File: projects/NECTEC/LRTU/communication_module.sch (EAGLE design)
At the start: 44 parts, among them Q1 BC847BS, U1 ESP-WROOM-32U (w/uFL), U2 IMAS980TH, U3 WG209_3E6, U4 RFM95W_SMT, X1 uFL, X2 uFL

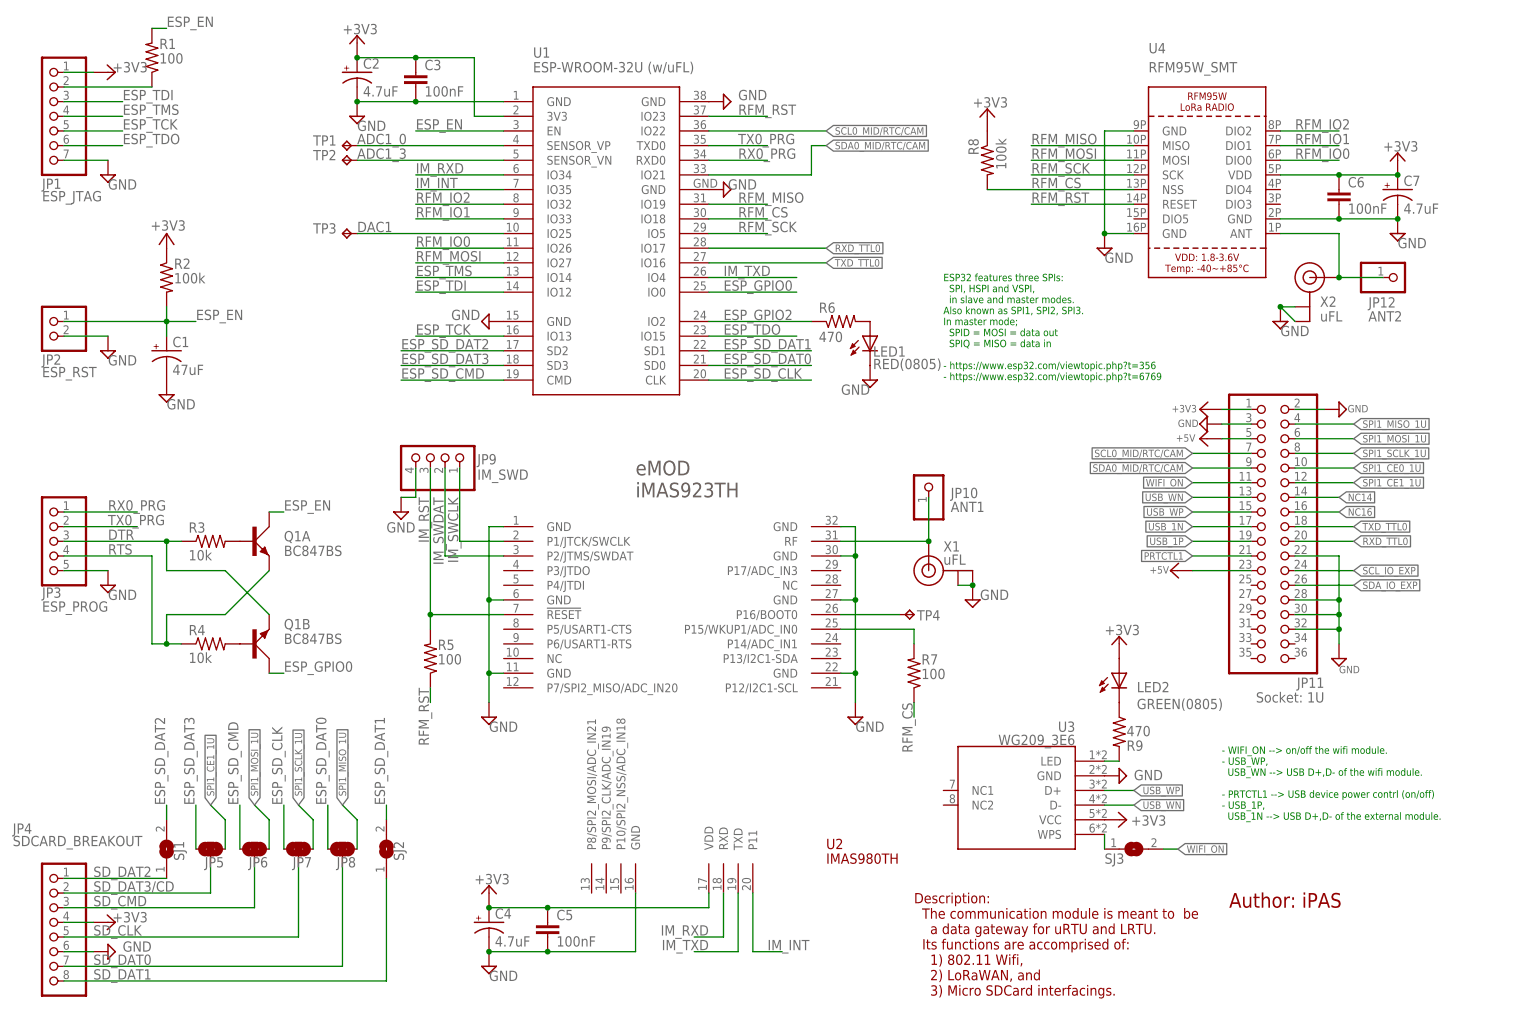
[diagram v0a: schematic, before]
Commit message: Fix ESP-eMOD connection, adding pull-up and swap uart pins.
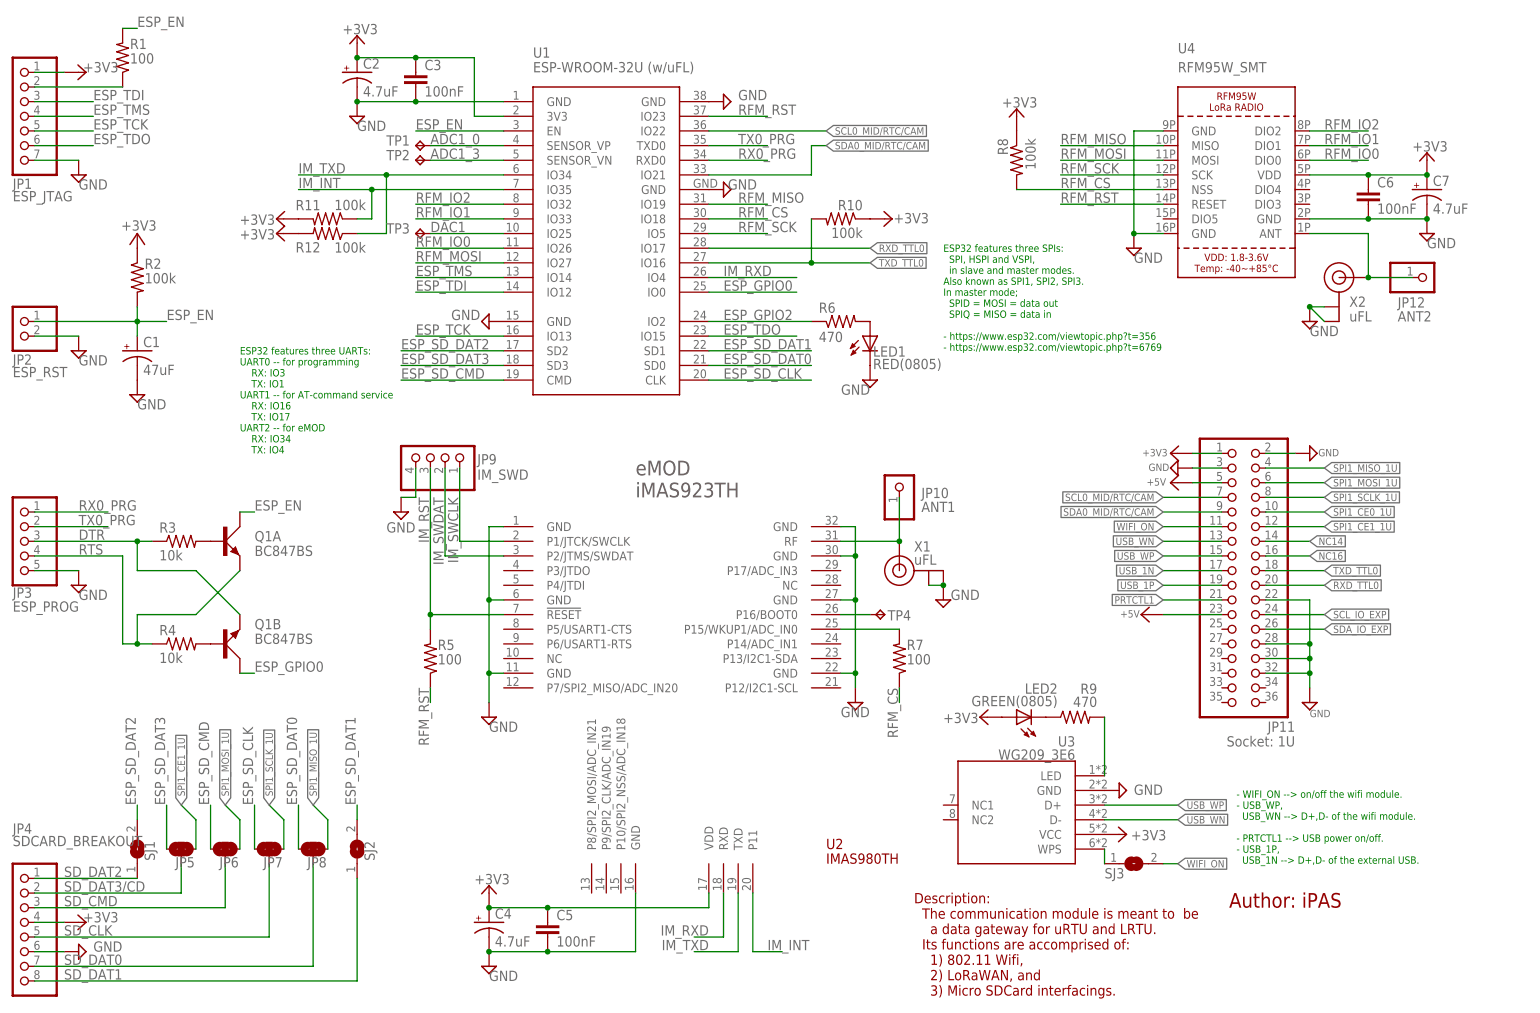
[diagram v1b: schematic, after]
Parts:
- added R10, R11, R12: 100k, ipas:RCL_R-USM0805
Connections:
- net +3V3: now also R10.1, R11.2, R12.2
- net IM_INT: now also R11.1
- net IM_RXD: now also U1.IO4; no longer U1.IO34
- net IM_TXD: now also R12.1, U1.IO34; no longer U1.IO4
- net TXD_TTL0: now also R10.2
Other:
- note added: "- WIFI_ON --> on/off the wifi module. - USB_WP, USB_WN --> D+,D- of the wifi module. - PRTCTL1 --> USB power on/off. - USB_1P, USB_1N --> D+,D- of the external USB."
- note added: "ESP32 features three UARTs: UART0 -- for programming RX: IO3 TX: IO1 UART1 -- for AT-command service RX: IO16 TX: IO17 UART2 -- for eMOD RX: IO34 TX: IO4"
- note removed: "- WIFI_ON --> on/off the wifi module. - USB_WP, USB_WN --> USB D+,D- of the wifi module. - PRTCTL1 --> USB device power contrl (on/off) - USB_1P, USB_1N --> USB D+,D- of the external module."
- moved on the sheet: C1, C6, C7, JP1, JP10, JP11, JP12, JP2, JP3, JP4, JP5, JP6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
